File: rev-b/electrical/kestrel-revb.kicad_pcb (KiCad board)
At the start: 4 copper layers, 136 x 106 mm, 351 parts, among them J1001 LCD RGB / contact fit pending, J1002 CAP TOUCH / contact fit pendi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, J1101 FOOT WIRE: 1SIGNAL 2GND, J1102 FOOT WIRE: 1SIGNAL 2GND, J201 NMJ4HCD2 INPUT, J202 NMJ4HCD2 OUTPUT, J401 PJ-102AH, J501 GOWIN JTAG / target VREF only, J701 UART / POWERED TARGET ONLY, Q401 AO4407A, SW501 RECONFIG / MPN pending, SW701 RESET / SMD button MPN pending, SW702 BOOT / SMD button MPN pending, U101 TPS54302DDCR, U102 TPS54302DDCR, U1101 SN74LVC1G17DCKR, U1102 SN74LVC1G17DCKR, U201 PCM1808PWR, U202 PCM5102APWR, U203 OPA1656IDR, U204 TLV76750DRVR, U205 TLV75533PDBVR, U206 TPS3808G01DBVR, U207 TPS3808G01DBVR, U301 TLV62569DBVR, U302 TPS3897ADRYR, U303 TPS22965DSGR, U501 GW2AR-LV18QN88C8/I7, U502 GD25Q32ESIGR, U503 SN74LVC1G125DCKR, U504 SN74LVC1G17DCKR, U601 TLV62569DBVR, U701 ESP32-P4NRW16X, U702 GD25Q32ESIGR, U801 SN74AXC4T774PWR, U802 TPS3808G01DBVR, U803 SN74LVC1G00DCKR, U901 TPS61169DCKR, U902 SN74LVC1G125DCKR, U903 TLV76701DRVR, U904 TLV76701DRVR, Y501 24.576MHz / 3.3V CMOS XO / MP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, Y701 40MHz / +/-10ppm / MPN and CL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

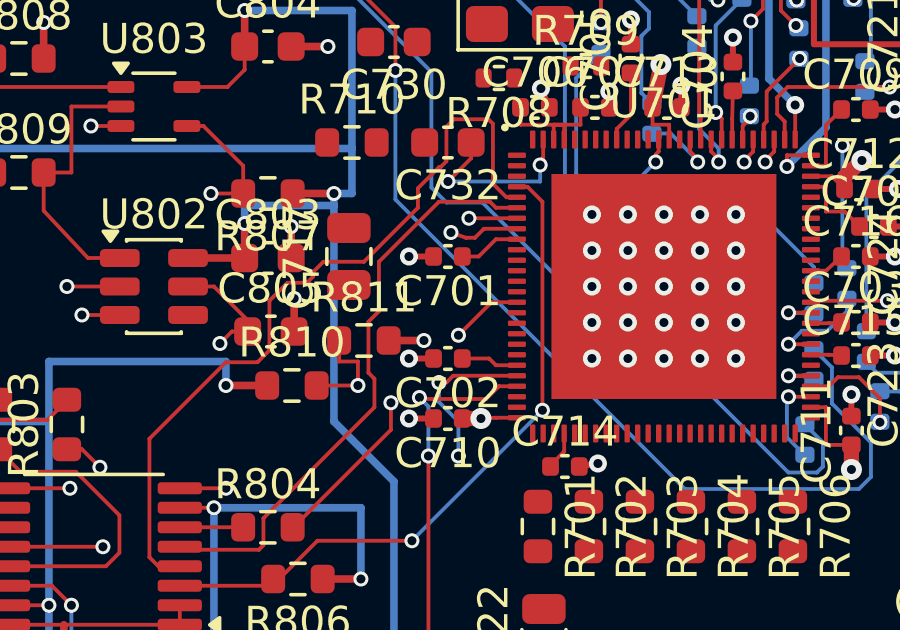
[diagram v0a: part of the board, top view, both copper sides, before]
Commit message: Reserve MCU fanout space with guarded HP and SPI routing changes
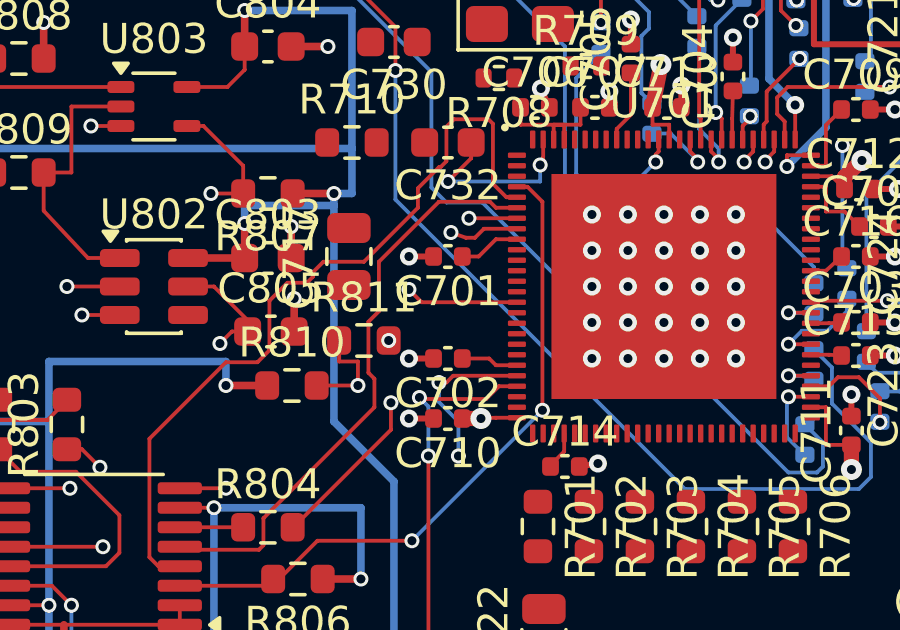
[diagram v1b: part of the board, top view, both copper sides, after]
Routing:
- net /MCU_RAW_MISO: track 11.1 -> 15.9 mm
- net /GND: track 212.5 -> 211.3 mm
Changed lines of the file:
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@@
 	)
 	(segment
-		(start 133 76.85)
-		(end 134.5 76.85)
-		(width 0.5)
+		(start 113.75 53.15)
+		(end 113.75 54.15)
+		(width 0.127)
 		(layer "F.Cu")
 		(net "/GND")
 	)
 	(segment
-		(start 113.75 53.15)
-		(end 113.75 54.15)
-		(width 0.127)
+		(start 133 76.85)
+		(end 134.5 76.85)
+		(width 0.5)
 		(layer "F.Cu")
 		(net "/GND")
@@
 	)
 	(segment
-		(start 114.825 87.8)
-		(end 116 87.8)
-		(width 0.254)
-		(layer "F.Cu")
-		(net "/GND")
-	)
-	(segment
 		(start 67.1375 112.65)
 		(end 66 112.65)
@@
 	)
 	(via
-		(at 116 87.8)
+		(at 114.825 87.8)
 		(size 0.5)
 		(drill 0.3)
@@
 	)
 	(segment
-		(start 129.3 91.15)
-		(end 130.25 92.1)
+		(start 130.6 81.8)
+		(end 129.3 83.1)
 		(width 0.508)
 		(layer "In2.Cu")
@@
 	)
 	(segment
-		(start 130.6 81.8)
-		(end 129.3 83.1)
+		(start 118.85 89.45)
+		(end 118.6 89.7)
+		(width 0.508)
+		(layer "In2.Cu")
+		(net "/ESP_VDD_HP")
+	)
+	(segment
+		(start 129.3 83.1)
+		(end 129.3 91.15)
 		(width 0.508)
 		(layer "In2.Cu")
@@
 	)
 	(segment
-		(start 118.6 89.7)
-		(end 117.9 90.4)
+		(start 118.85 78.25)
+		(end 118.85 89.45)
 		(width 0.508)
 		(layer "In2.Cu")
@@
 	(segment
 		(start 118.6 78)
-		(end 118.6 89.7)
+		(end 118.85 78.25)
 		(width 0.508)
 		(layer "In2.Cu")
@@
 	)
 	(segment
-		(start 129.3 83.1)
-		(end 129.3 91.15)
+		(start 118.6 89.7)
+		(end 117.9 90.4)
+		(width 0.508)
+		(layer "In2.Cu")
+		(net "/ESP_VDD_HP")
+	)
+	(segment
+		(start 129.3 91.15)
+		(end 130.25 92.1)
 		(width 0.508)
 		(layer "In2.Cu")
@@
 	(segment
 		(start 119.1 86.525)
-		(end 118.25 86.525)
+		(end 115.925 86.525)
 		(width 0.127)
 		(layer "F.Cu")
@@
 	)
 	(segment
-		(start 111.65 94.025)
-		(end 111.625 94.025)
+		(start 114.9 90.775)
+		(end 111.65 94.025)
 		(width 0.127)
 		(layer "F.Cu")
@@
 	)
 	(segment
-		(start 118.25 86.525)
-		(end 117.15 87.625)
+		(start 115.925 86.525)
+		(end 115.5 86.1)
 		(width 0.127)
 		(layer "F.Cu")
@@
 	)
 	(segment
-		(start 114.9 90.775)
-		(end 111.65 94.025)
+		(start 111.65 94.025)
+		(end 111.625 94.025)
 		(width 0.127)
 		(layer "F.Cu")
@@
 	)
 	(via
-		(at 117.15 87.625)
+		(at 115.5 86.1)
 		(size 0.5)
 		(drill 0.3)
@@
 	)
 	(segment
-		(start 117.15 87.625)
+		(start 115.5 86.1)
+		(end 117.35 86.1)
+		(width 0.127)
+		(layer "In2.Cu")
+		(net "/MCU_RAW_MISO")
+	)
+	(segment
+		(start 117.35 86.1)
+		(end 117.35 87.425)
+		(width 0.127)
+		(layer "In2.Cu")
+		(net "/MCU_RAW_MISO")
+	)
+	(segment
+		(start 117.35 87.425)
 		(end 114.9 89.875)
 		(width 0.127)
